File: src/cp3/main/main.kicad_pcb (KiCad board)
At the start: 2 copper layers, 40.3 x 108.2 mm, 68 parts, among them J1 PJ398SM, J2 PJ398SM, J3 PJ398SM, J4 PJ398SM, J5 PJ398SM, J6 PJ398SM, J7 IDC_Header, Q1 THAT340, Q10 MMBT3904, Q5 MMBT3904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

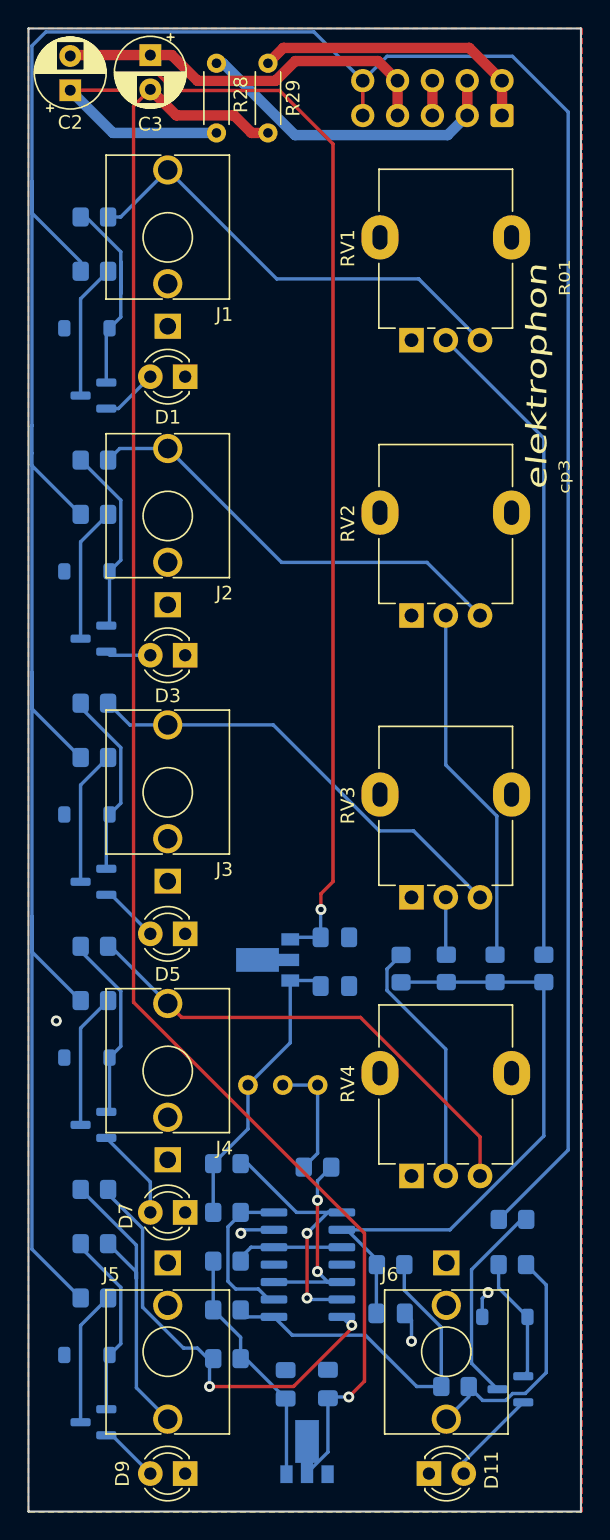
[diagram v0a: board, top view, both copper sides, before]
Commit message: update to Kicad8
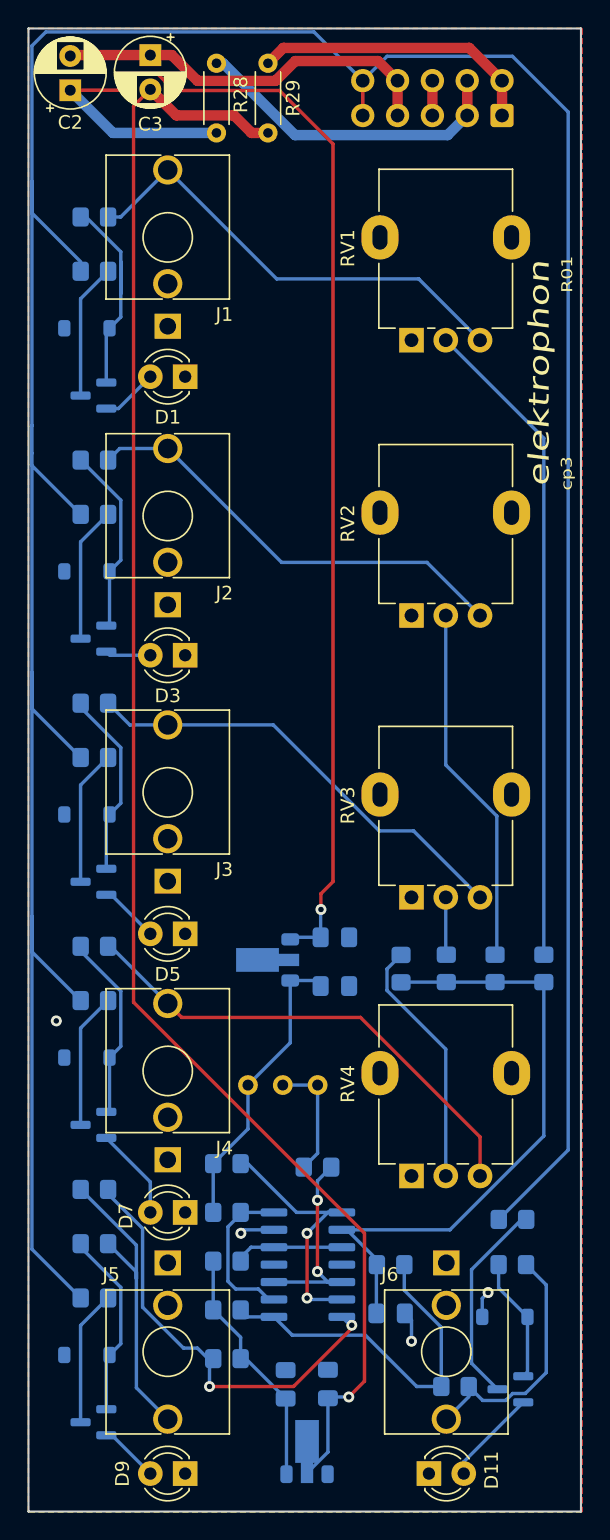
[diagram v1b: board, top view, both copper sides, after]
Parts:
- moved REF** 0.29 mm to (89.1, 76.0)
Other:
- board text added: "cp3"
